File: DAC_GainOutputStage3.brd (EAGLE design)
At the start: 110 x 85.8 mm, 55 parts, among them J1 1935190, J3 SJ-63033A

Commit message: Finished schematic and working layout
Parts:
- removed C10O: 0.1uF, 35V, Dual Mono Amp Library:MKS4B031002A00JC00
- removed R7O: 1M*, Dual Mono Amp Library:RESAD1540W60L620D230
- added C2O1: 0.1uF, 35V, Dual Mono Amp Library:MKS4B031002A00JC00
- added D4, D5, D6: (no value), adafruit:DO-1N4148
- added R10, R16: 48.7, rcl:0207/10
- added R11, R12: 9.1k, rcl:0207/10
- added R13, R14: 1k, rcl:0207/10
- added R15: 330, rcl:0207/10
- added R3O1: 1M*, Dual Mono Amp Library:RESAD1540W60L620D230
- added U1, U2: V_REG_317SMD, SparkFun-IC-Power:SOT223
- added Z1, Z2: 1N750, 1N750:DIOAD1256W56L444D203
- moved SX4 132.8 mm to (88.5, 60.5), turned to 162 degrees
- moved R3 115.5 mm to (119.0, -50.0)
- moved C4 94.9 mm to (75.0, -52.0)
- moved C2 88.6 mm to (75.0, -42.0)
- moved SX3 85.1 mm to (21.5, 60.5), turned to 342 degrees
- moved R4 74.5 mm to (78.0, -60.0)
- moved C1 50.7 mm to (17.0, -36.0)
- moved C3 50.7 mm to (17.0, -56.0)
- moved D1 50.7 mm to (18.0, -98.0)
- moved D2 50.7 mm to (18.0, -101.0)
- moved D3 50.7 mm to (18.0, -104.0)
- moved R1 50.7 mm to (19.0, -15.0)
- moved R2 50.7 mm to (19.0, -20.0)
- moved R5 50.7 mm to (19.0, -74.0)
- moved R6 50.7 mm to (19.0, -79.0)
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- renumbered C7O to C21O1
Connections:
- new net N$29: D6.A, R13.1, SX2.7
- new net N$37: R10.2, U1.2
- new net N$38: R16.2, U2.2
- net +240VDC: now also C2O1.1, R11.2, R12.2, SX2.9; no longer SX2.6
- net AGND: now also R10.1, R15.1, R16.1, R3O1.2, U1.1, U2.1; no longer C10O.2, R7O.2
- net L+: now also R4.2; no longer R4.1
- net L-: now also R3.2; no longer R3.1
- net L_OUT: no longer R7O.1
- net N$14: now also R14.1, SX2.2, Z2.2; no longer R3.2, SX4.2
- net N$17: now also C2O1.2, R14.2, R3O1.1; no longer R4.2, SX4.7
- net N$2: now also Z1.2
- net N$22: now also U1.3
- net N$26: now also Z1.1
- net N$27: now also R15.2, SX2.3, Z2.1; no longer SX4.3, SX4.6
- net N$3: now also C21O1.2, D6.C, SX2.1, SX2.6; no longer SX2.7
- net N$4: now also D4.A, R3.1, SX4.2; no longer SX2.8
- net N$5: now also D5.A, R4.1, SX4.7; no longer C21O1.2, SX2.1
- net N$7: now also D4.C, D5.C, SX4.3, SX4.6, U2.3; no longer SX2.2
- net N$8: now also R11.1, SX4.1; no longer SX2.3
- net N$9: now also R12.1, R13.2, SX4.9; no longer C10O.1, SX2.9
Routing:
- net 66.3VAC/1: track 123.6 -> 0.00 mm
- net 66.3VAC/2: track 118.2 -> 0.00 mm
- net R-: track 87.3 -> 0.00 mm, vias 1 -> 0
- net L-: track 98.1 -> 13.5 mm
- net N$5: track 64.5 -> 0.00 mm
- net L_OUT: track 51.5 -> 0.00 mm
- net N$18: track 39.2 -> 0.00 mm
- net +240VDC: track 37.2 -> 0.00 mm
- net N$8: track 26.3 -> 0.00 mm
- net N$3: track 23.7 -> 0.00 mm
- net L+: track 33.4 -> 10.7 mm
- net R+: track 32.3 -> 10.7 mm
- net R_OUT: track 20.2 -> 0.00 mm
- net N$4: track 9.01 -> 0.00 mm
- net N$9: track 6.99 -> 0.00 mm
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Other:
- board size 110 x 85.8 mm -> 110 x 96.8 mm

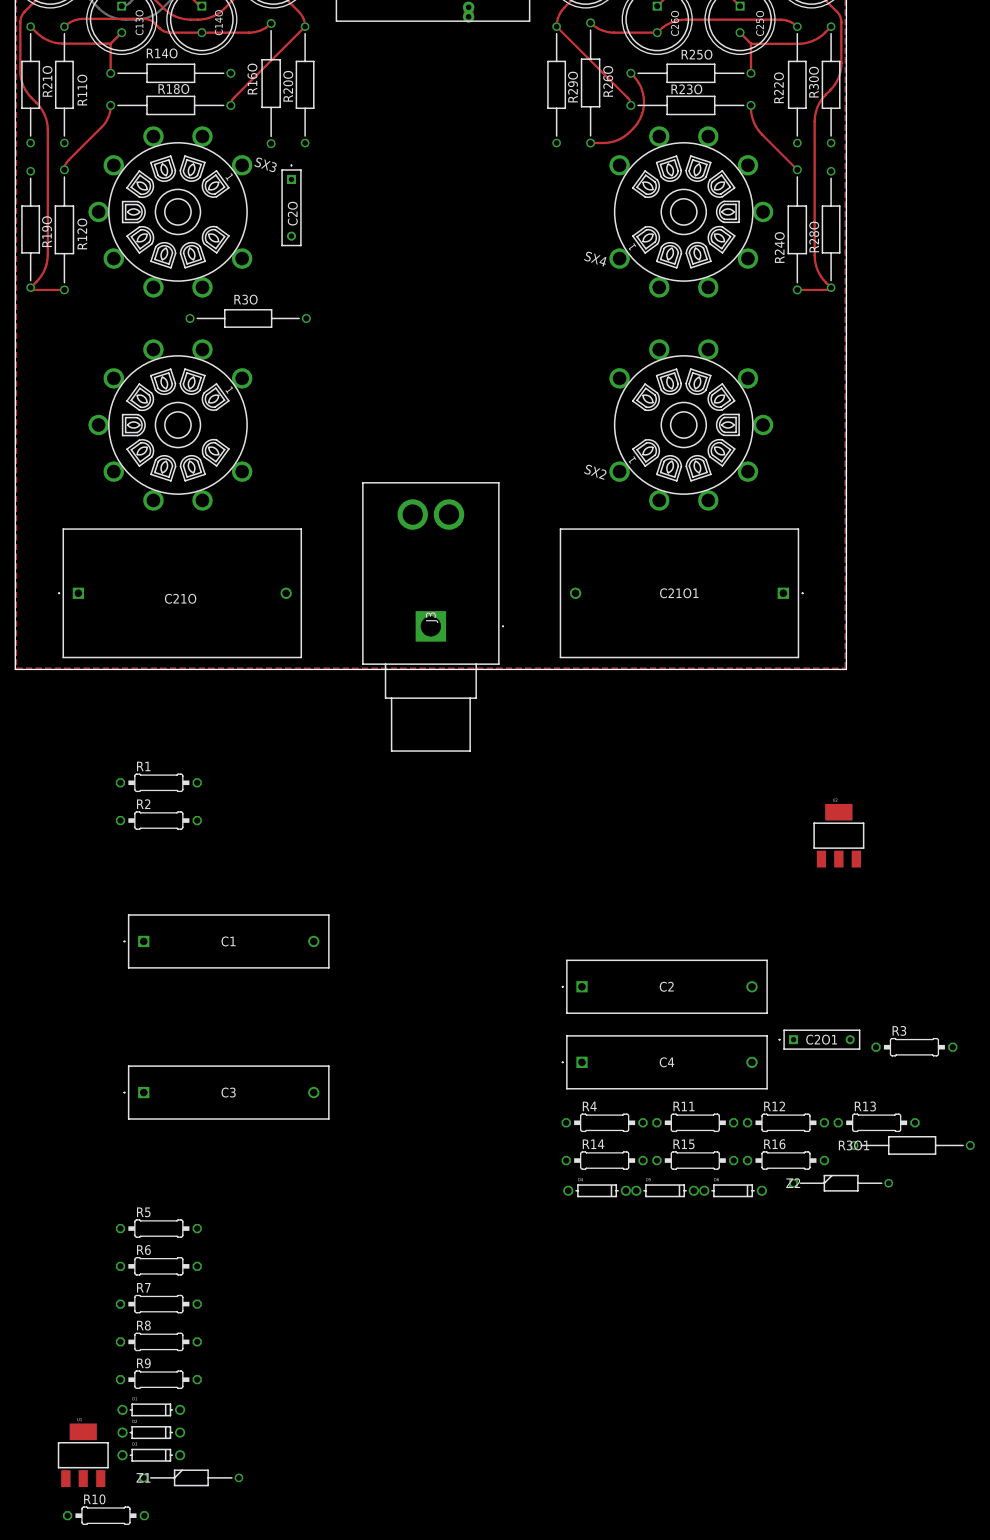
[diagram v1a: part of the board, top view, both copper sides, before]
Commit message: Fixed schematic
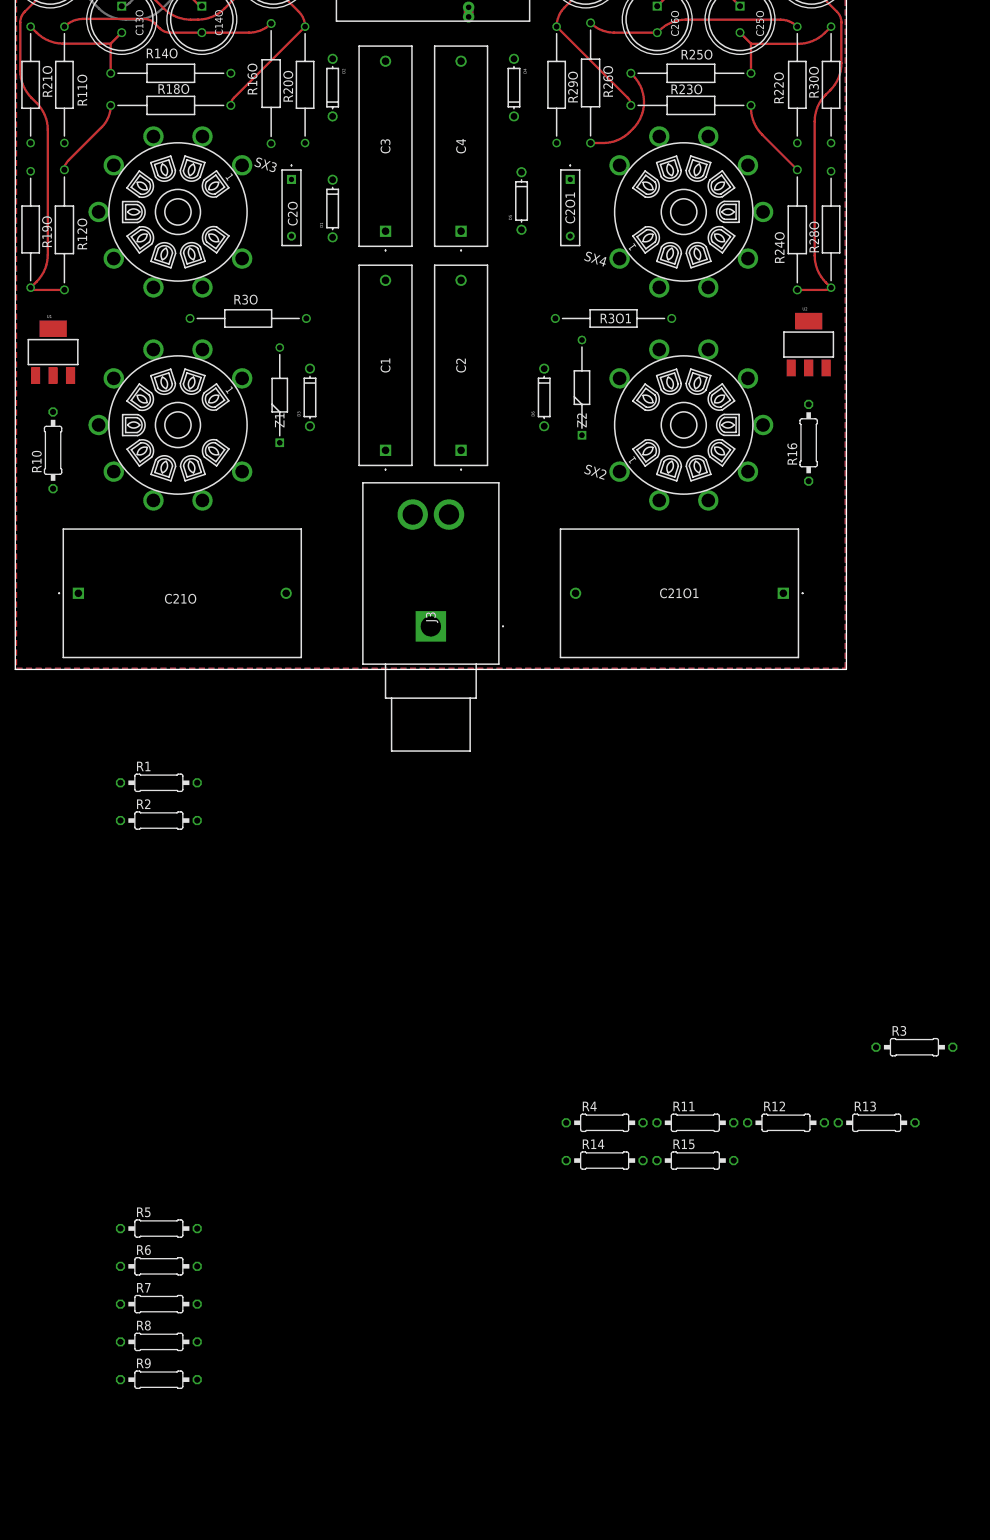
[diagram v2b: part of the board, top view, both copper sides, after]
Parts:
- moved D2 179.6 mm to (42.0, 77.0), turned to 270 degrees
- moved D1 160.8 mm to (42.0, 61.0), turned to 90 degrees
- moved D4 146.4 mm to (66.0, 77.0), turned to 270 degrees
- moved U1 146.1 mm to (5.00, 42.0)
- moved D3 141.6 mm to (39.0, 36.0), turned to 90 degrees
- moved R10 141.2 mm to (5.00, 29.0), turned to 90 degrees
- moved Z1 138.2 mm to (35.0, 30.0), turned to 90 degrees
- moved D5 132.4 mm to (67.0, 62.0), turned to 90 degrees
- moved C3 118.4 mm to (49.0, 58.0), turned to 90 degrees
- moved C2O1 117.6 mm to (73.4, 64.8), turned to 270 degrees
- moved R3O1 116.4 mm to (71.5, 46.5)
- moved C4 111.2 mm to (59.0, 58.0), turned to 90 degrees
- moved D6 107.9 mm to (70.0, 36.0), turned to 90 degrees
- moved Z2 102.9 mm to (75.0, 31.0), turned to 90 degrees
- moved R16 95.0 mm to (105.0, 30.0), turned to 90 degrees
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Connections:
- net +240VDC: now also SX1.6, SX2.6; no longer SX1.9, SX2.9
- net N$18: now also SX1.8; no longer SX1.6
- net N$3: now also SX2.8; no longer SX2.6

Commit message: Progress
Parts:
- moved R7 135.0 mm to (21.0, 51.0)
- moved R6 134.1 mm to (36.0, 54.0)
- moved R8 128.3 mm to (37.0, 38.0), turned to 90 degrees
- moved R3 126.6 mm to (73.0, 68.0), turned to 90 degrees
- moved R5 123.2 mm to (36.0, 48.0)
- moved R9 118.3 mm to (42.0, 22.0), turned to 90 degrees
- moved R12 117.5 mm to (73.3, 53.9), turned to 180 degrees
- moved R13 115.0 mm to (88.0, 52.0), turned to 180 degrees
- moved R4 114.1 mm to (102.2, 51.5)
- moved R11 110.5 mm to (72.9, 49.2), turned to 180 degrees
- moved R14 103.1 mm to (74.0, 38.0), turned to 90 degrees
- moved R15 90.7 mm to (68.0, 23.0), turned to 90 degrees
- moved R1 84.9 mm to (37.0, 68.0), turned to 90 degrees
- moved R2 72.8 mm to (8.00, 52.0), turned to 180 degrees
- moved R3O1 13.0 mm to (84.5, 46.5)
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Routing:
- net N$11: track 47.5 -> 45.2 mm
- net N$20: track 47.4 -> 45.1 mm
- net N$28: track 17.2 -> 18.6 mm
- net N$36: track 17.2 -> 18.6 mm
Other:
- board size 110 x 96.8 mm -> 110 x 102.8 mm

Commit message: Update DAC_GainOutputStage3.brd
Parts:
- moved D4 14.0 mm to (67.2, 69.0), turned to 90 degrees
- moved D5 14.0 mm to (67.2, 83.0), turned to 270 degrees
- moved C2O 7.10 mm to (42.1, 58.2), turned to 180 degrees
- moved R6 2.48 mm to (36.9, 51.7)
- moved R12 2.21 mm to (73.1, 51.7)
- moved R11 2.01 mm to (73.1, 47.2)
- moved R7 1.66 mm to (22.5, 51.7)
- moved R15 1.52 mm to (68.0, 21.5)
- moved R3O1 1.32 mm to (83.4, 47.2)
- moved R5 1.22 mm to (36.9, 47.2)
- moved R16 1.07 mm to (104.6, 29.0)
- moved U2 1.07 mm to (104.6, 42.0)
- moved R2 0.94 mm to (7.11, 51.7)
- moved D6 0.89 mm to (73.9, 26.0)
- moved R8 0.89 mm to (36.1, 38.0)
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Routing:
- net +240VDC: track 0.00 -> 130.9 mm
- net 66.3VAC/1: track 0.00 -> 73.0 mm
- net 66.3VAC/2: track 0.00 -> 72.4 mm
- net R_OUT: track 0.00 -> 52.1 mm
- net L_OUT: track 0.00 -> 52.1 mm
- net N$18: track 0.00 -> 41.5 mm
- net N$3: track 0.00 -> 37.6 mm
- net N$29: track 0.00 -> 32.2 mm
- net N$6: track 0.00 -> 26.1 mm
- net N$7: track 0.00 -> 24.4 mm
- net N$22: track 0.00 -> 24.4 mm
- net N$4: track 0.00 -> 23.2 mm
- net R-: track 0.00 -> 21.3 mm
- net N$23: track 0.00 -> 20.6 mm
- net N$2: track 0.00 -> 12.3 mm
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
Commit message: Finished routing
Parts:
- removed SH1: SHORTA5, Dual Mono Amp Library:SHORT_ALL-50
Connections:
- removed net DGND: J1.4, SH1.1
- net AGND: now also J1.4; no longer SH1.2
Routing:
- net 66.3VAC/2: track 72.4 -> 197.2 mm
- net 66.3VAC/1: track 73.0 -> 186.0 mm
- net +240VDC: track 130.9 -> 235.4 mm
- net N$13: track 7.92 -> 76.2 mm
- net N$5: track 0.00 -> 61.3 mm
- net N$7: track 24.4 -> 77.6 mm
- net N$22: track 24.4 -> 74.8 mm
- net N$9: track 4.26 -> 49.6 mm, vias 0 -> 1
- net N$23: track 20.6 -> 51.1 mm
- net N$35: track 0.00 -> 30.2 mm
- net N$26: track 3.92 -> 32.4 mm
- net N$27: track 3.92 -> 31.2 mm
- net R+: track 10.7 -> 32.0 mm
- net L+: track 10.7 -> 32.1 mm
- net N$14: track 12.3 -> 29.3 mm
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- added copper zone on layer 1, net AGND
- removed copper zone on layer 1, net DGND

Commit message: Progress
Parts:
- removed Z1, Z2: 1N750, 1N750:DIOAD1256W56L444D203
- added Z3, Z4: 1N750, Dual Mono Amp Library:DIOAD1256W56L444D203
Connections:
- net N$14: now also Z4.2; no longer Z2.2
- net N$2: now also Z3.2; no longer Z1.2
- net N$26: now also Z3.1; no longer Z1.1
- net N$27: now also Z4.1; no longer Z2.1
